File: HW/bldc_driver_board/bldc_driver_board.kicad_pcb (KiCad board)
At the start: 2 copper layers, 56 parts, among them IC1 DRV8305NPHPR, J1 PWR, J2 N_CN7, J3 N_CN10, J4 HALL, J5 Motor, J6 RJ45, J7 RJ45, Q1 STD140N6F7, Q2 STD140N6F7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

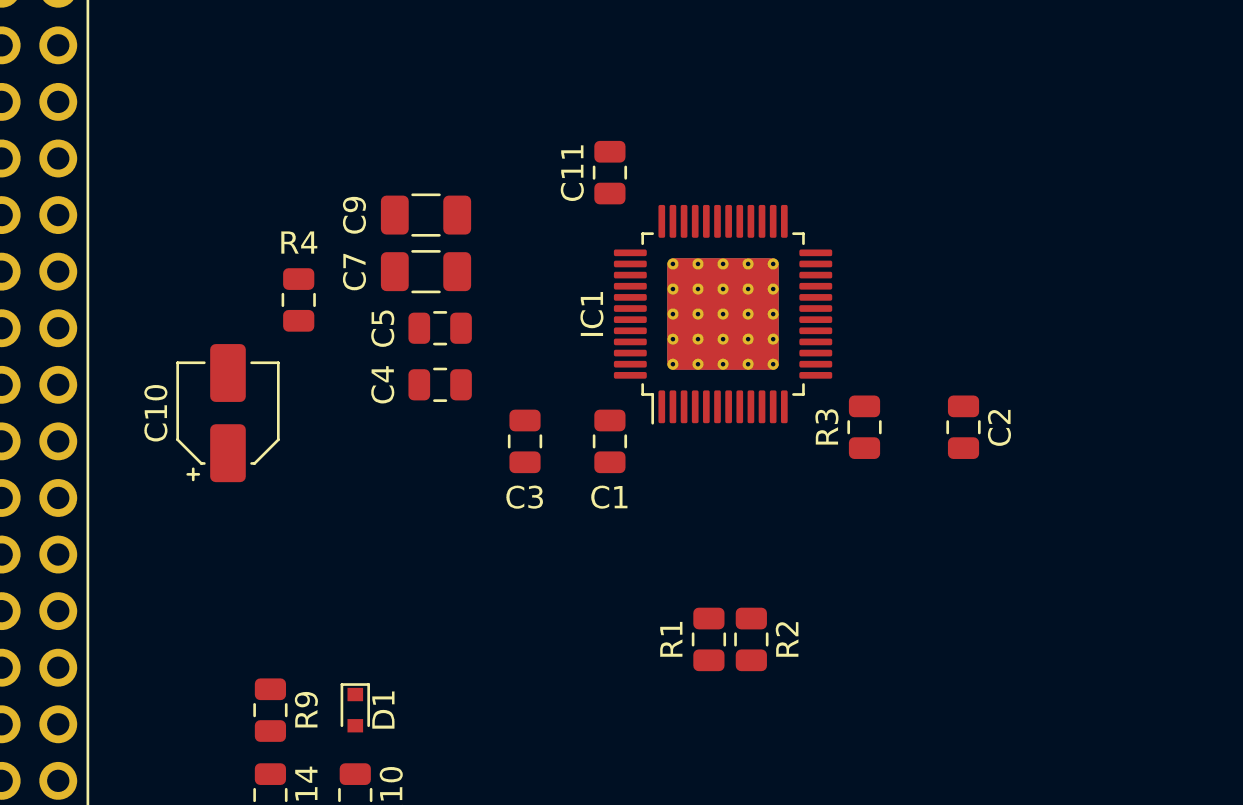
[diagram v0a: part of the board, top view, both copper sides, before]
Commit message: -- Added elecrow design rules
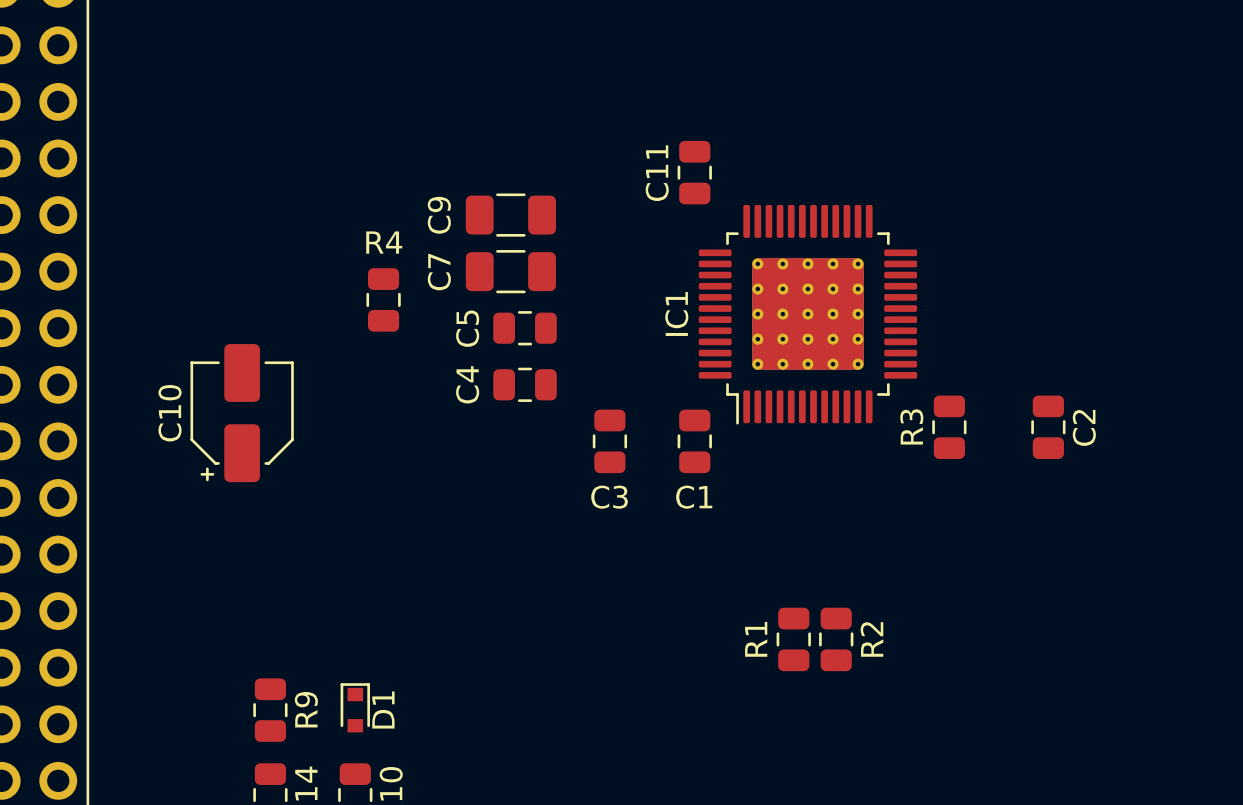
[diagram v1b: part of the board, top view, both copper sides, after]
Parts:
- moved C7 3.81 mm to (66.0, 109.2)
- moved C9 3.81 mm to (66.0, 106.7)
- moved C1 3.81 mm to (74.3, 116.8)
- moved C11 3.81 mm to (74.3, 104.8)
- moved C2 3.81 mm to (90.2, 116.2)
- moved C3 3.81 mm to (70.5, 116.8)
- moved IC1 3.81 mm to (79.4, 111.1)
- moved R2 3.81 mm to (80.6, 125.7)
- moved R4 3.81 mm to (60.3, 110.5)
- moved C4 3.81 mm to (66.7, 114.3)
- moved C5 3.81 mm to (66.7, 111.8)
- moved R1 3.81 mm to (78.7, 125.7)
- moved R3 3.81 mm to (85.7, 116.2)
- moved C10 0.63 mm to (54.0, 115.6)
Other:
- net class Default: clearance 0.2 -> 0.1778; trace_width 0.25 -> 0.2032; via_dia 0.8 -> 0.635; via_drill 0.4 -> 0.3048
- rule trace_clearance: 0.2 -> 0.1778
- rule trace_min: 0.2 -> 0.2032
- rule via_min_drill: 0.3 -> 0.3048
- rule via_min_size: 0.4 -> 0.635
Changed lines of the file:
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@@
   )
   (setup
-    (last_trace_width 0.25)
-    (trace_clearance 0.2)
+    (last_trace_width 0.2032)
+    (user_trace_width 0.2032)
+    (user_trace_width 0.4064)
+    (user_trace_width 0.8128)
+    (user_trace_width 1.6256)
+    (trace_clearance 0.1778)
     (zone_clearance 0.508)
     (zone_45_only no)
-    (trace_min 0.2)
+    (trace_min 0.2032)
     (segment_width 0.2)
     (edge_width 0.1)
-    (via_size 0.8)
-    (via_drill 0.4)
-    (via_min_size 0.4)
-    (via_min_drill 0.3)
-    (uvia_size 0.3)
-    (uvia_drill 0.1)
+    (via_size 0.635)
+    (via_drill 0.3048)
+    (via_min_size 0.635)
+    (via_min_drill 0.3048)
+    (user_via 0.635 0.3048)
+    (uvia_size 0.508)
+    (uvia_drill 0.127)
     (uvias_allowed no)
     (uvia_min_size 0.2)
@@
   (net 116 "Net-(U1-Pad8)")
   (net_class Default "Dies ist die voreingestellte Netzklasse."
-    (clearance 0.2)
-    (trace_width 0.25)
-    (via_dia 0.8)
-    (via_drill 0.4)
-    (uvia_dia 0.3)
-    (uvia_drill 0.1)
+    (clearance 0.1778)
+    (trace_width 0.2032)
+    (via_dia 0.635)
+    (via_drill 0.3048)
+    (uvia_dia 0.508)
+    (uvia_drill 0.127)
+    (diff_pair_gap 0.25)
+    (diff_pair_width 0.25)
     (add_net +12V)
     (add_net +5V)
@@
   )
   (module Capacitor_SMD:C_0805_2012Metric (layer F.Cu)
-    (at 70.485 116.84 270)
+    (at 74.295 116.84 270)
     (descr "Capacitor SMD 0805 (2012 Metric), square (rectangular) end terminal, IPC_7351 nominal, (Body size source: https://docs.google.com/spreadsheets/d/1BsfQQcO9C6DZCsRaXUlFlo91Tg2WpOkGARC1WS5S8t0/edit?usp=sharing), generated with kicad-footprint-generator")
     (tags capacitor)
@@
   )
   (module Capacitor_SMD:C_0805_2012Metric (layer F.Cu)
-    (at 86.36 116.205 270)
+    (at 90.17 116.205 270)
     (descr "Capacitor SMD 0805 (2012 Metric), square (rectangular) end terminal, IPC_7351 nominal, (Body size source: https://docs.google.com/spreadsheets/d/1BsfQQcO9C6DZCsRaXUlFlo91Tg2WpOkGARC1WS5S8t0/edit?usp=sharing), generated with kicad-footprint-generator")
     (tags capacitor)
@@
   )
   (module Capacitor_SMD:C_0805_2012Metric (layer F.Cu)
-    (at 66.675 116.84 90)
+    (at 70.485 116.84 90)
     (descr "Capacitor SMD 0805 (2012 Metric), square (rectangular) end terminal, IPC_7351 nominal, (Body size source: https://docs.google.com/spreadsheets/d/1BsfQQcO9C6DZCsRaXUlFlo91Tg2WpOkGARC1WS5S8t0/edit?usp=sharing), generated with kicad-footprint-generator")
     (tags capacitor)
@@
   )
   (module Capacitor_SMD:C_0805_2012Metric (layer F.Cu)
-    (at 62.865 114.3 180)
+    (at 66.675 114.3 180)
     (descr "Capacitor SMD 0805 (2012 Metric), square (rectangular) end terminal, IPC_7351 nominal, (Body size source: https://docs.google.com/spreadsheets/d/1BsfQQcO9C6DZCsRaXUlFlo91Tg2WpOkGARC1WS5S8t0/edit?usp=sharing), generated with kicad-footprint-generator")
     (tags capacitor)
@@
   )
   (module Capacitor_SMD:C_0805_2012Metric (layer F.Cu)
-    (at 62.865 111.76)
+    (at 66.675 111.76)
     (descr "Capacitor SMD 0805 (2012 Metric), square (rectangular) end terminal, IPC_7351 nominal, (Body size source: https://docs.google.com/spreadsheets/d/1BsfQQcO9C6DZCsRaXUlFlo91Tg2WpOkGARC1WS5S8t0/edit?usp=sharing), generated with kicad-footprint-generator")
     (tags capacitor)
@@
   )
   (module Capacitor_SMD:C_1206_3216Metric (layer F.Cu)
-    (at 62.23 109.22)
+    (at 66.04 109.22)
     (descr "Capacitor SMD 1206 (3216 Metric), square (rectangular) end terminal, IPC_7351 nominal, (Body size source: http://www.tortai-tech.com/upload/download/2011102023233369053.pdf), generated with kicad-footprint-generator")
     (tags capacitor)
@@
   )
   (module Capacitor_SMD:C_1206_3216Metric (layer F.Cu)
-    (at 62.23 106.68)
+    (at 66.04 106.68)
     (descr "Capacitor SMD 1206 (3216 Metric), square (rectangular) end terminal, IPC_7351 nominal, (Body size source: http://www.tortai-tech.com/upload/download/2011102023233369053.pdf), generated with kicad-footprint-generator")
     (tags capacitor)
@@
   )
   (module Capacitor_SMD:CP_Elec_4x5.8 (layer F.Cu)
-    (at 53.34 115.57 90)
+    (at 53.975 115.57 90)
     (descr "SMD capacitor, aluminum electrolytic, Panasonic, 4.0x5.8mm")
     (tags "capacitor electrolytic")
@@
   )
   (module Capacitor_SMD:C_0805_2012Metric (layer F.Cu)
-    (at 70.485 104.775 90)
+    (at 74.295 104.775 90)
     (descr "Capacitor SMD 0805 (2012 Metric), square (rectangular) end terminal, IPC_7351 nominal, (Body size source: https://docs.google.com/spreadsheets/d/1BsfQQcO9C6DZCsRaXUlFlo91Tg2WpOkGARC1WS5S8t0/edit?usp=sharing), generated with kicad-footprint-generator")
     (tags capacitor)
@@
   )
   (module Package_QFP:TQFP-48-1EP_7x7mm_P0.5mm_EP5x5mm_ThermalVias (layer F.Cu)
-    (at 75.565 111.125 90)
+    (at 79.375 111.125 90)
     (descr "TQFP, 48 Pin (https://www.trinamic.com/fileadmin/assets/Products/ICs_Documents/TMC2100_datasheet_Rev1.08.pdf (page 45)), generated with kicad-footprint-generator ipc_qfp_generator.py")
     (tags "TQFP QFP")
@@
   )
   (module Resistor_SMD:R_0805_2012Metric (layer F.Cu)
-    (at 74.93 125.73 90)
+    (at 78.74 125.73 90)
     (descr "Resistor SMD 0805 (2012 Metric), square (rectangular) end terminal, IPC_7351 nominal, (Body size source: https://docs.google.com/spreadsheets/d/1BsfQQcO9C6DZCsRaXUlFlo91Tg2WpOkGARC1WS5S8t0/edit?usp=sharing), generated with kicad-footprint-generator")
     (tags resistor)
@@
   )
   (module Resistor_SMD:R_0805_2012Metric (layer F.Cu)
-    (at 76.835 125.73 270)
+    (at 80.645 125.73 270)
     (descr "Resistor SMD 0805 (2012 Metric), square (rectangular) end terminal, IPC_7351 nominal, (Body size source: https://docs.google.com/spreadsheets/d/1BsfQQcO9C6DZCsRaXUlFlo91Tg2WpOkGARC1WS5S8t0/edit?usp=sharing), generated with kicad-footprint-generator")
     (tags resistor)
@@
   )
   (module Resistor_SMD:R_0805_2012Metric (layer F.Cu)
-    (at 81.915 116.205 90)
+    (at 85.725 116.205 90)
     (descr "Resistor SMD 0805 (2012 Metric), square (rectangular) end terminal, IPC_7351 nominal, (Body size source: https://docs.google.com/spreadsheets/d/1BsfQQcO9C6DZCsRaXUlFlo91Tg2WpOkGARC1WS5S8t0/edit?usp=sharing), generated with kicad-footprint-generator")
     (tags resistor)
@@
   )
   (module Resistor_SMD:R_0805_2012Metric (layer F.Cu)
-    (at 56.515 110.49 270)
+    (at 60.325 110.49 270)
     (descr "Resistor SMD 0805 (2012 Metric), square (rectangular) end terminal, IPC_7351 nominal, (Body size source: https://docs.google.com/spreadsheets/d/1BsfQQcO9C6DZCsRaXUlFlo91Tg2WpOkGARC1WS5S8t0/edit?usp=sharing), generated with kicad-footprint-generator")
     (tags resistor)

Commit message: -- Continued pcb layout
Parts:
- moved C19 26.7 mm to (104.1, 141.0), turned to 270 degrees
- moved R5 23.2 mm to (72.4, 143.5)
- moved JP1 21.9 mm to (69.8, 143.5)
- moved D2 20.3 mm to (80.0, 143.5)
- moved R2 8.84 mm to (72.3, 122.9)
- moved R4 8.64 mm to (65.4, 117.5), turned to 0 degrees
- moved U1 8.60 mm to (93.6, 141.0), turned to 180 degrees
- moved R1 5.36 mm to (74.2, 122.9)
- moved C9 1.80 mm to (64.8, 105.4)
- moved C7 1.80 mm to (64.8, 108.0)
- moved C10 1.27 mm to (55.2, 115.6)
- moved C2 1.27 mm to (88.9, 116.2)
- moved C4 1.27 mm to (65.4, 114.3)
- moved C5 1.27 mm to (65.4, 111.8)
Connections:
- J2 pad 28: /SO1F -> /SO1
- J2 pad 30: /SO2F -> /SO2
- J2 pad 32: /SO3F -> /SO3
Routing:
- net GND: track 0.00 -> 160.2 mm
- net +BATT: track 0.00 -> 148.3 mm, vias 0 -> 2
- net /~FAULT: track 0.00 -> 68.6 mm, vias 0 -> 2
- net /SO3: track 0.00 -> 61.8 mm, vias 0 -> 1
- net /SO2: track 0.00 -> 58.7 mm, vias 0 -> 1
- net /SO1: track 0.00 -> 55.6 mm, vias 0 -> 1
- net /SDO: track 0.00 -> 54.3 mm, vias 0 -> 3
- net /SDI: track 0.00 -> 52.1 mm, vias 0 -> 2
- net /CAN_L: track 0.00 -> 47.4 mm
- net /INHA: track 0.00 -> 41.3 mm
- net /INHB: track 0.00 -> 41.0 mm
- net /INHC: track 0.00 -> 37.7 mm, vias 0 -> 1
- net /INLA: track 0.00 -> 37.5 mm, vias 0 -> 1
- net /EN_GATE: track 0.00 -> 36.8 mm
- net /CAN_H: track 0.00 -> 36.5 mm
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
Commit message: -- Continued PCB design
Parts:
- moved C22 29.2 mm to (87.6, 108.1), turned to 90 degrees
- moved C20 28.8 mm to (87.6, 100.7), turned to 90 degrees
- moved C21 21.5 mm to (87.6, 104.4), turned to 90 degrees
- moved C10 1.63 mm to (54.2, 116.8), turned to 0 degrees
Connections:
- J5 pad 1: /SHA -> /SHC
- J5 pad 3: /SHC -> /SHA
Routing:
- net GND: track 160.2 -> 239.9 mm, vias 0 -> 1
- net +12V: track 0.76 -> 77.1 mm, vias 0 -> 2
- net /SLA: track 0.00 -> 9.81 mm
- net /SLB: track 0.00 -> 7.43 mm
- net /SLC: track 0.00 -> 4.86 mm

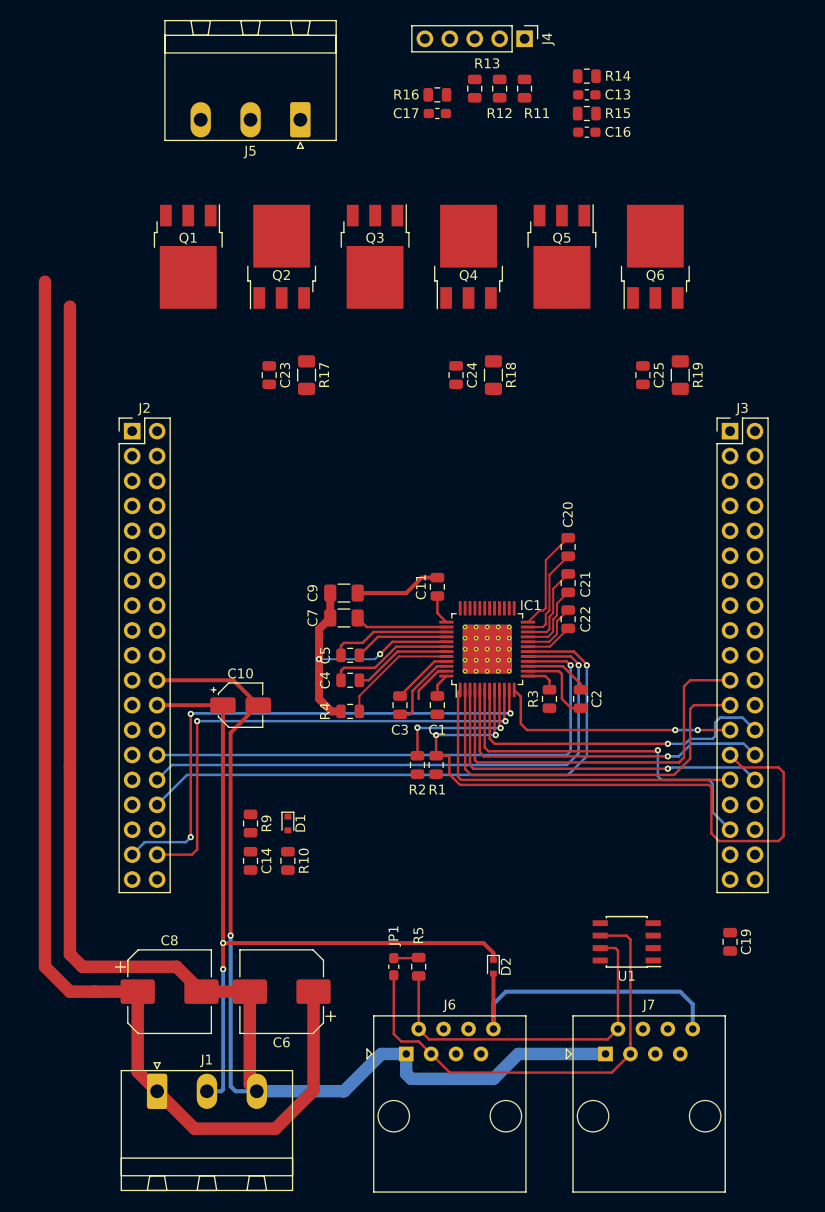
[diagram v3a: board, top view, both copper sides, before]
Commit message: -- Continued routing and removed MOSFET Capacitors
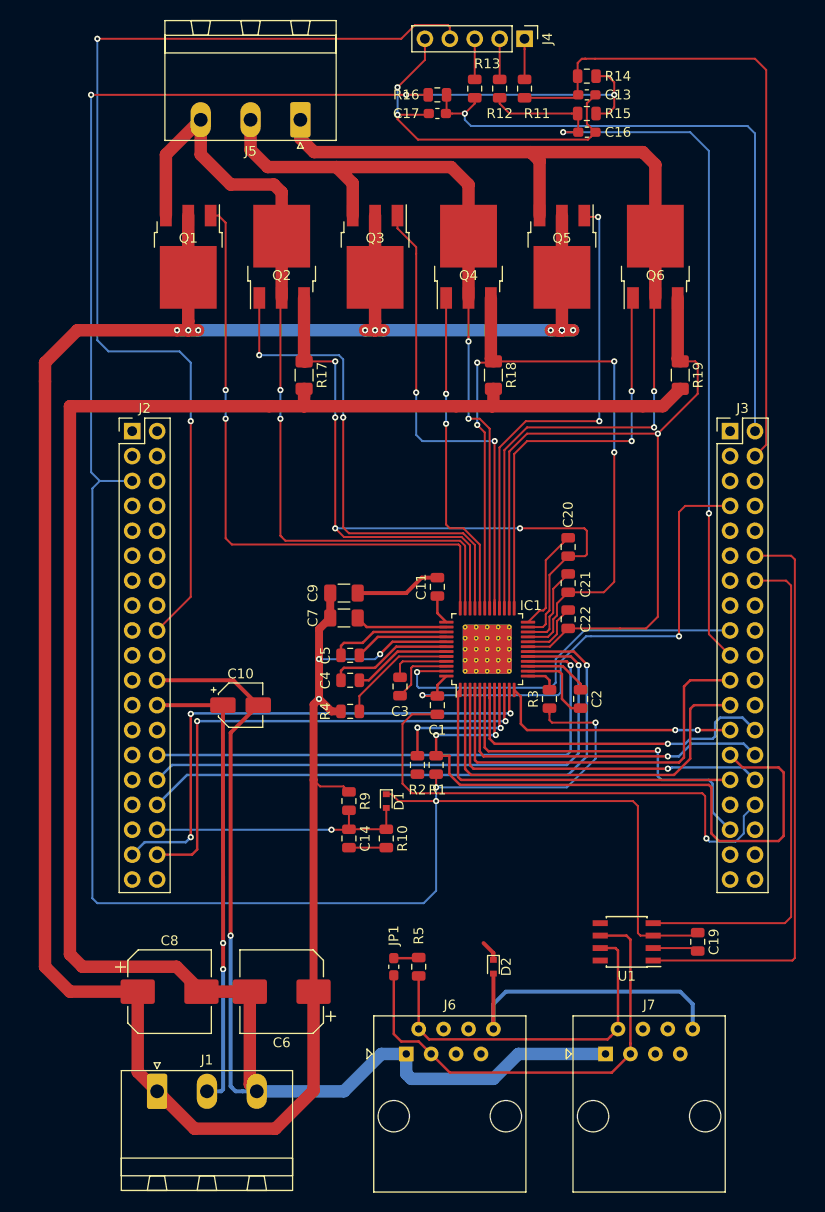
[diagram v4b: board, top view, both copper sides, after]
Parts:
- removed C23, C24, C25: 220nF, Capacitor_SMD:C_0805_2012Metric
- moved C14 10.3 mm to (65.3, 130.4)
- moved R9 10.3 mm to (65.3, 126.6)
- moved D1 10.3 mm to (69.1, 126.6)
- moved R10 10.3 mm to (69.1, 130.4)
- moved C19 3.30 mm to (100.8, 141.0)
- moved C3 1.91 mm to (70.5, 114.9)
- moved R17 0.25 mm to (60.7, 83.2)
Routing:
- net VDD: track 0.00 -> 268.5 mm, vias 0 -> 6
- net +BATT: track 148.3 -> 271.3 mm, vias 2 -> 14
- net +5V: track 0.00 -> 107.7 mm, vias 0 -> 2
- net /SHC: track 0.00 -> 105.2 mm, vias 0 -> 2
- net GND: track 239.9 -> 343.3 mm, vias 1 -> 3
- net /SHA: track 0.00 -> 85.3 mm, vias 0 -> 2
- net /HALL_B: track 0.00 -> 80.4 mm, vias 0 -> 2
- net /SLA: track 9.81 -> 88.2 mm, vias 0 -> 4
- net /SHB: track 0.00 -> 77.9 mm, vias 0 -> 2
- net /SLC: track 4.86 -> 82.3 mm, vias 0 -> 1
- net /SLB: track 7.43 -> 81.0 mm, vias 0 -> 4
- net /HALL_A: track 0.00 -> 68.7 mm
- net /HALL_C: track 0.00 -> 67.0 mm, vias 0 -> 1
- net /GHA: track 0.00 -> 64.6 mm, vias 0 -> 2
- net /CAN_TX: track 0.00 -> 59.4 mm
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
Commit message: -- Added borders
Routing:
- net GND: track 343.3 -> 342.3 mm
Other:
- board outline added: 80 x 119.4 mm
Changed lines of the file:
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@@
   (general
     (thickness 1.6)
-    (drawings 2)
+    (drawings 4)
     (tracks 696)
     (zones 0)
@@
     )
   )
-  (dimension 120.015 (width 0.3) (layer F.SilkS)
-    (gr_text "120,015 mm" (at 17.585 106.9975 270) (layer F.SilkS)
-      (effects (font (size 1.5 1.5) (thickness 0.3)))
-    )
-    (feature1 (pts (xy 46.355 167.005) (xy 19.098579 167.005)))
-    (feature2 (pts (xy 46.355 46.99) (xy 19.098579 46.99)))
-    (crossbar (pts (xy 19.685 46.99) (xy 19.685 167.005)))
-    (arrow1a (pts (xy 19.685 167.005) (xy 19.098579 165.878496)))
-    (arrow1b (pts (xy 19.685 167.005) (xy 20.271421 165.878496)))
-    (arrow2a (pts (xy 19.685 46.99) (xy 19.098579 48.116504)))
-    (arrow2b (pts (xy 19.685 46.99) (xy 20.271421 48.116504)))
-  )
-  (dimension 63.5 (width 0.3) (layer F.SilkS)
-    (gr_text "63,500 mm" (at 74.93 29.65) (layer F.SilkS)
-      (effects (font (size 1.5 1.5) (thickness 0.3)))
-    )
-    (feature1 (pts (xy 106.68 88.9) (xy 106.68 31.163579)))
-    (feature2 (pts (xy 43.18 88.9) (xy 43.18 31.163579)))
-    (crossbar (pts (xy 43.18 31.75) (xy 106.68 31.75)))
-    (arrow1a (pts (xy 106.68 31.75) (xy 105.553496 32.336421)))
-    (arrow1b (pts (xy 106.68 31.75) (xy 105.553496 31.163579)))
-    (arrow2a (pts (xy 43.18 31.75) (xy 44.306504 32.336421)))
-    (arrow2b (pts (xy 43.18 31.75) (xy 44.306504 31.163579)))
-  )
+  (gr_line (start 31.75 166.37) (end 31.75 46.99) (layer Edge.Cuts) (width 0.1))
+  (gr_line (start 111.76 166.37) (end 31.75 166.37) (layer Edge.Cuts) (width 0.1))
+  (gr_line (start 111.76 46.99) (end 111.76 166.37) (layer Edge.Cuts) (width 0.1))
+  (gr_line (start 31.75 46.99) (end 111.76 46.99) (layer Edge.Cuts) (width 0.1))
   (segment (start 75.2125 113.875) (end 74.295 114.7925) (width 0.254) (layer F.Cu) (net 1))
   (segment (start 74.295 114.7925) (end 74.295 115.9025) (width 0.254) (layer F.Cu) (net 1))
@@
   (segment (start 96.299 141.605) (end 100.5355 141.605) (width 0.2032) (layer F.Cu) (net 4))
   (segment (start 97.285 86.36) (end 99.06 84.585) (width 1.27) (layer F.Cu) (net 4))
-  (segment (start 36.83 142.24) (end 36.83 86.36) (width 1.27) (layer F.Cu) (net 4))
-  (segment (start 38.1 143.51) (end 36.83 142.24) (width 1.27) (layer F.Cu) (net 4))
-  (segment (start 50.24 146.05) (end 47.7 143.51) (width 1.27) (layer F.Cu) (net 4))
-  (segment (start 47.7 143.51) (end 38.1 143.51) (width 1.27) (layer F.Cu) (net 4))
   (segment (start 60.706 85.31) (end 60.706 86.36) (width 1.27) (layer F.Cu) (net 4))
   (segment (start 60.706 84.585) (end 60.706 85.31) (width 1.27) (layer F.Cu) (net 4))
@@
   (segment (start 60.706 86.36) (end 76.2 86.36) (width 1.27) (layer F.Cu) (net 4))
   (segment (start 76.2 86.36) (end 79.883 86.36) (width 1.27) (layer F.Cu) (net 4))
-  (segment (start 36.83 86.36) (end 57.15 86.36) (width 1.27) (layer F.Cu) (net 4))
-  (segment (start 57.15 86.36) (end 60.706 86.36) (width 1.27) (layer F.Cu) (net 4))
   (via (at 70.231 53.848) (size 0.635) (drill 0.3048) (layers F.Cu B.Cu) (net 4))
   (segment (start 73.025 48.895) (end 73.025 51.054) (width 0.2032) (layer F.Cu) (net 4))
@@
   (segment (start 89.535 57.545) (end 90.41 58.42) (width 0.2032) (layer F.Cu) (net 4))
   (segment (start 89.535 55.485) (end 89.535 57.545) (width 0.2032) (layer F.Cu) (net 4))
+  (segment (start 47.7 143.51) (end 50.24 146.05) (width 1.27) (layer F.Cu) (net 4))
+  (segment (start 38.1 143.51) (end 47.7 143.51) (width 1.27) (layer F.Cu) (net 4))
+  (segment (start 36.83 142.24) (end 38.1 143.51) (width 1.27) (layer F.Cu) (net 4))
+  (segment (start 36.83 88.011) (end 36.83 142.24) (width 1.27) (layer F.Cu) (net 4))
+  (segment (start 60.706 86.36) (end 38.481 86.36) (width 1.27) (layer F.Cu) (net 4))
+  (segment (start 38.481 86.36) (end 36.83 88.011) (width 1.27) (layer F.Cu) (net 4))
   (segment (start 75.2125 112.875) (end 71.783 112.875) (width 0.2032) (layer F.Cu) (net 5))
   (segment (start 71.783 112.875) (end 71.628 113.03) (width 0.2032) (layer F.Cu) (net 5))
